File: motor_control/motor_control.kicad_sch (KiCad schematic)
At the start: 20 parts, among them J1 GPIO, J2 Conn_01x06_Pin, J3 Conn_01x06_Pin, J4 Conn_01x02_Pin, SW1 PULLUP, SW2 PULLDOWN, U1 HC-SR04

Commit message: finish up schematic
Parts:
- removed A1: RaspberryPi_Pico, Module:RaspberryPi_Pico_Common_Unspecified, symbol MCU_Module:RaspberryPi_Pico
- added A3: RaspberryPi_Pico, Module:RaspberryPi_Pico_Common_Unspecified, symbol RaspberryPi_Pico:RaspberryPi_Pico
- added J5: Conn_UART, symbol Connector:Conn_01x02_Pin
- added J6: Conn_SPI, symbol Connector:Conn_01x04_Pin
- added J7: Conn_I2C, symbol Connector:Conn_01x02_Pin
- SW1: value PULLUP -> PU
- SW2: value PULLDOWN -> PD
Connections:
- net +3V3: now also SW2.1, A3.36 (3V3(OUT)); no longer SW2.2
- net +5V: no longer U1.1 (VCC)
- net AIN1: now also A3.20 (GP15)
- net AIN2: now also A3.19 (GP14)
- net BIN1: now also A3.21 (GP16)
- net BIN2: now also A3.22 (GP17)
- net BLUE: now also A3.31 (GP26_ADC0)
- net C1A: now also A3.15 (GP11)
- net C1B: now also A3.25 (GP19)
- net C2A: now also A3.14 (GP10)
- net C2B: now also A3.26 (GP20)
- net ECHO: now also A3.12 (GP9)
- net GND: now also C1.1, A3.13 (GND), A3.18 (GND), A3.23 (GND), A3.28 (GND), A3.3 (GND), A3.33 (AGND), A3.38 (GND), A3.8 (GND); no longer C1.2
- net GREEN: now also A3.32 (GP27_ADC1)
- net PULLDOWN: now also SW2.2, A3.29 (GP22); no longer SW2.1
- net PULLUP: now also C1.2, A3.27 (GP21); no longer C1.1
- net PWMA: now also A3.17 (GP13)
- net PWMB: now also A3.24 (GP18)
- net RED: now also A3.34 (GP28_ADC2)
- net STBY: now also A3.16 (GP12)
- net TRIG: now also A3.11 (GP8)
- net VBUS: now also U1.1 (VCC), A3.40 (VBUS)
- net VSYS: now also A3.39 (VSYS)
- net GPIO2/SDA1 renamed SDA1
- net SDA1: now also A3.9 (GP6), J7.1 (Pin_1)
- net GPIO3/SCL1 renamed SCL1
- net SCL1: now also A3.10 (GP7), J7.2 (Pin_2)
- new net ADC_VREF: A3.35 (ADC_VREF)
- new net SPI0_CSn: A3.7 (GP5), J6.4 (Pin_4)
- new net SPI0_RX: A3.6 (GP4), J6.3 (Pin_3)
- new net SPI0_SCK: A3.4 (GP2), J6.1 (Pin_1)
- new net SPI0_TX: A3.5 (GP3), J6.2 (Pin_2)
- new net UART0_RX: A3.2 (GP1), J5.2 (Pin_2)
- new net UART0_TX: A3.1 (GP0), J5.1 (Pin_1)
- no-connect marks 0 -> 2
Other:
- moved on the sheet: A2, C1, C2, D1, J2, J3, J4, R1, R2, R3, R4, R5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

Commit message: assign footprints to capacitors
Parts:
- C1, C2: footprint (none) -> Capacitor_THT:C_Disc_D4.7mm_W2.5mm_P5.00mm
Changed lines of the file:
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@@
 			)
 		)
-		(property "Footprint" ""
+		(property "Footprint" "Capacitor_THT:C_Disc_D4.7mm_W2.5mm_P5.00mm"
 			(at 164.1348 149.86 0)
 			(effects
@@
 			)
 		)
-		(property "Footprint" ""
+		(property "Footprint" "Capacitor_THT:C_Disc_D4.7mm_W2.5mm_P5.00mm"
 			(at 194.6148 139.7 0)
 			(effects

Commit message: assign footprints to resistors
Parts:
- R1, R2, R3, R4, R5, R6, R7: footprint (none) -> Resistor_THT:R_Axial_DIN0207_L6.3mm_D2.5mm_P7.62mm_Horizontal
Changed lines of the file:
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@@
 			)
 		)
-		(property "Footprint" ""
+		(property "Footprint" "Resistor_THT:R_Axial_DIN0207_L6.3mm_D2.5mm_P7.62mm_Horizontal"
 			(at 231.14 150.368 90)
 			(effects
@@
 			)
 		)
-		(property "Footprint" ""
+		(property "Footprint" "Resistor_THT:R_Axial_DIN0207_L6.3mm_D2.5mm_P7.62mm_Horizontal"
 			(at 197.358 153.67 90)
 			(effects
@@
 			)
 		)
-		(property "Footprint" ""
+		(property "Footprint" "Resistor_THT:R_Axial_DIN0207_L6.3mm_D2.5mm_P7.62mm_Horizontal"
 			(at 223.52 123.952 90)
 			(effects
@@
 			)
 		)
-		(property "Footprint" ""
+		(property "Footprint" "Resistor_THT:R_Axial_DIN0207_L6.3mm_D2.5mm_P7.62mm_Horizontal"
 			(at 231.14 160.528 90)
 			(effects
@@
 			)
 		)
-		(property "Footprint" ""
+		(property "Footprint" "Resistor_THT:R_Axial_DIN0207_L6.3mm_D2.5mm_P7.62mm_Horizontal"
 			(at 223.52 129.032 90)
 			(effects
@@
 			)
 		)
-		(property "Footprint" ""
+		(property "Footprint" "Resistor_THT:R_Axial_DIN0207_L6.3mm_D2.5mm_P7.62mm_Horizontal"
 			(at 166.878 143.51 90)
 			(effects
@@
 			)
 		)
-		(property "Footprint" ""
+		(property "Footprint" "Resistor_THT:R_Axial_DIN0207_L6.3mm_D2.5mm_P7.62mm_Horizontal"
 			(at 231.14 155.448 90)
 			(effects

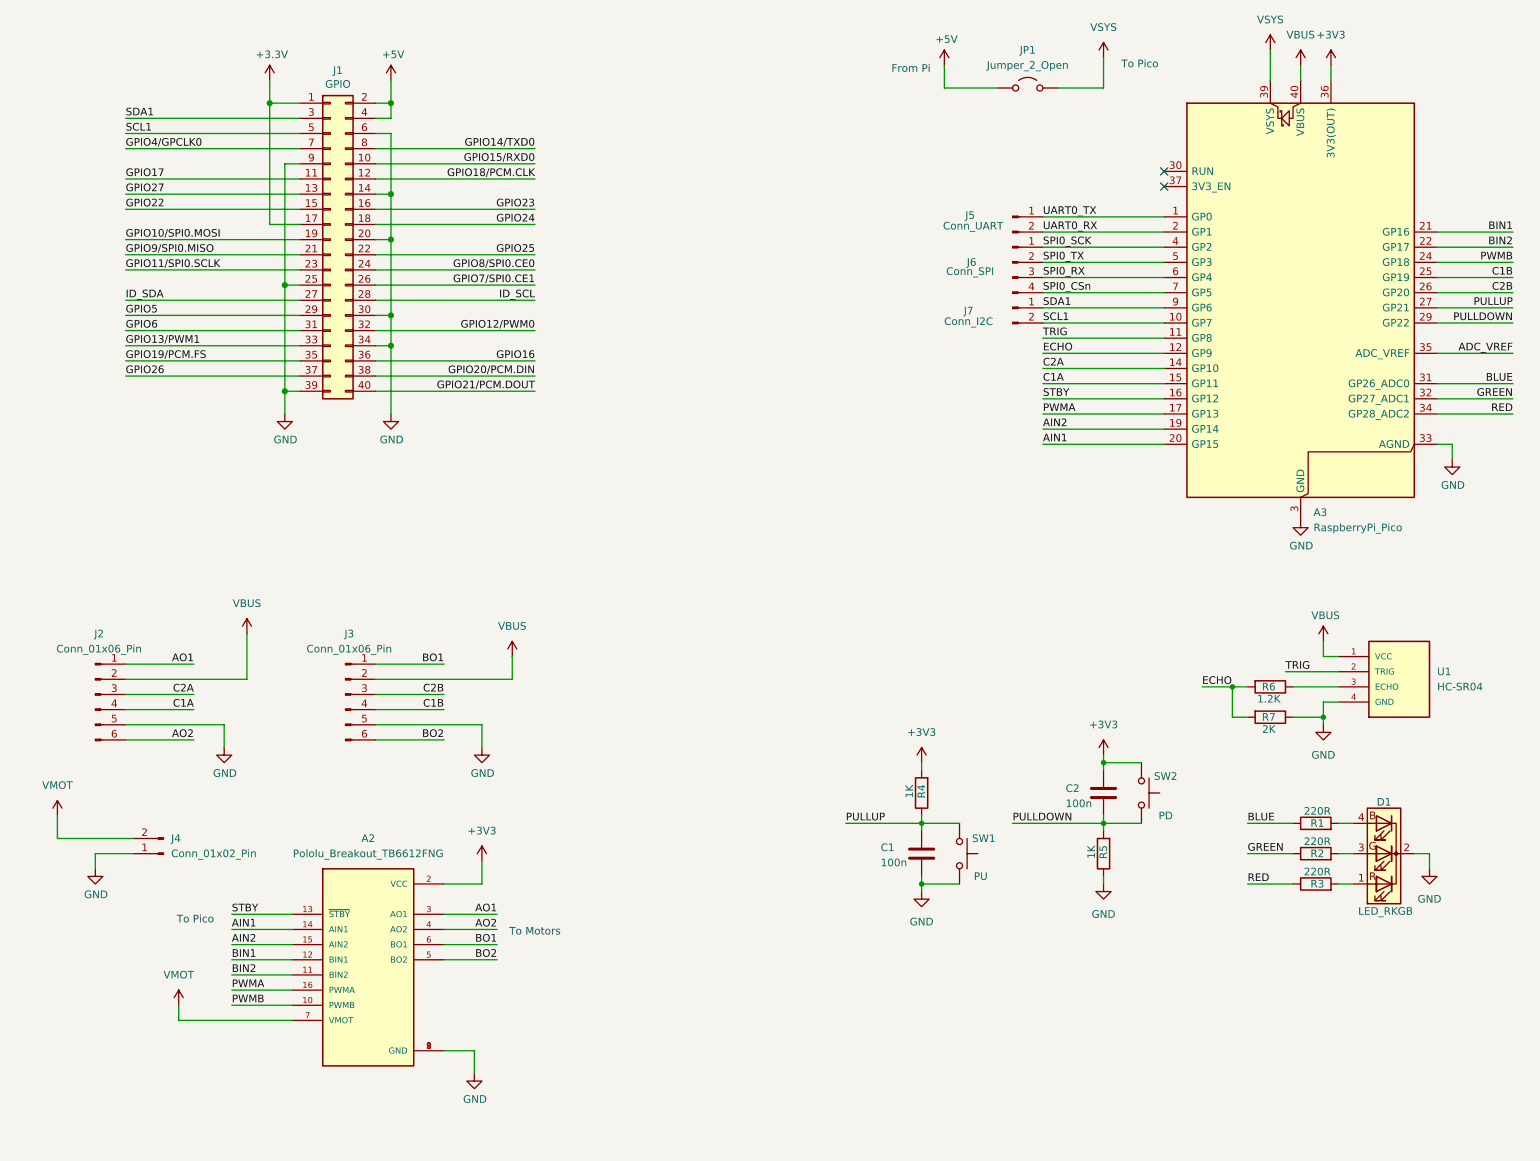
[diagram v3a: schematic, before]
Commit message: assign footprints to more parts
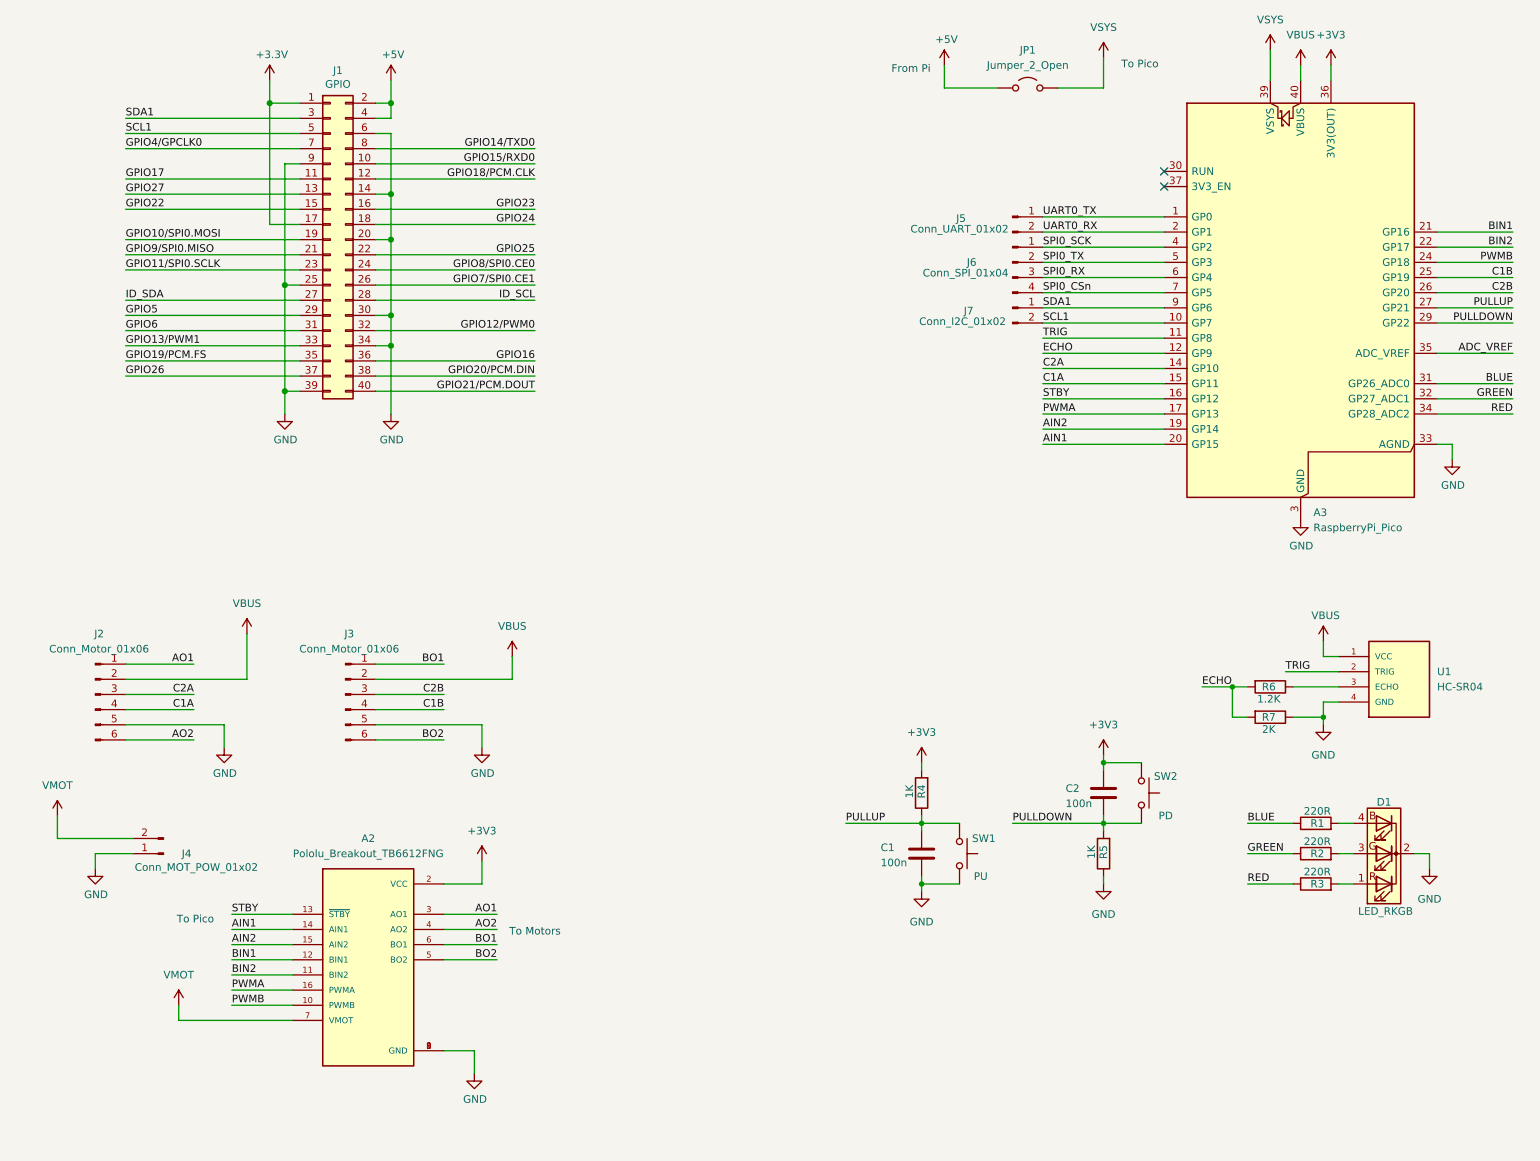
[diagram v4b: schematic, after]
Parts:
- D1: footprint (none) -> LED_THT:LED_D5.0mm-4_RGB_Wide_Pins
- J2, J3: value Conn_01x06_Pin -> Conn_Motor_01x06; footprint (none) -> Connector_PinHeader_2.54mm:PinHeader_1x06_P2.54mm_Vertical
- J4: value Conn_01x02_Pin -> Conn_MOT_POW_01x02; footprint (none) -> Connector_PinHeader_2.54mm:PinHeader_1x02_P2.54mm_Horizontal
- J5: value Conn_UART -> Conn_UART_01x02; footprint (none) -> Connector_PinHeader_2.54mm:PinHeader_1x02_P2.54mm_Vertical
- J6: value Conn_SPI -> Conn_SPI_01x04; footprint (none) -> Connector_PinHeader_2.54mm:PinHeader_1x04_P2.54mm_Vertical
- J7: value Conn_I2C -> Conn_I2C_01x02; footprint (none) -> Connector_PinHeader_2.54mm:PinHeader_1x02_P2.54mm_Vertical
- JP1: footprint (none) -> Connector_PinHeader_2.54mm:PinHeader_1x02_P2.54mm_Vertical
- SW1, SW2: footprint (none) -> Button_Switch_THT:SW_PUSH_6mm
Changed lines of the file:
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@@
 		(on_board yes)
 		(dnp no)
-		(fields_autoplaced yes)
 		(property "Reference" "J4"
-			(at 39.37 151.1299 0)
+			(at 41.148 153.67 0)
 			(effects
 				(font
@@
 			)
 		)
-		(property "Value" "Conn_01x02_Pin"
-			(at 39.37 153.6699 0)
+		(property "Value" "Conn_MOT_POW_01x02"
+			(at 33.274 155.956 0)
 			(effects
 				(font
@@
 			)
 		)
-		(property "Footprint" ""
+		(property "Footprint" "Connector_PinHeader_2.54mm:PinHeader_1x02_P2.54mm_Horizontal"
 			(at 38.1 153.67 0)
 			(effects
@@
 			)
 		)
-		(property "Footprint" ""
+		(property "Footprint" "LED_THT:LED_D5.0mm-4_RGB_Wide_Pins"
 			(at 242.57 152.4 0)
 			(effects
@@
 			)
 		)
-		(property "Value" "Conn_I2C"
-			(at 172.974 64.516 0)
-			(effects
-				(font
-					(size 1.27 1.27)
-				)
-			)
-		)
-		(property "Footprint" ""
+		(property "Value" "Conn_I2C_01x02"
+			(at 171.958 64.516 0)
+			(effects
+				(font
+					(size 1.27 1.27)
+				)
+			)
+		)
+		(property "Footprint" "Connector_PinHeader_2.54mm:PinHeader_1x02_P2.54mm_Vertical"
 			(at 180.34 62.23 0)
 			(effects
@@
 			)
 		)
-		(property "Footprint" ""
+		(property "Footprint" "Button_Switch_THT:SW_PUSH_6mm"
 			(at 207.01 143.51 0)
 			(effects
@@
 			)
 		)
-		(property "Value" "Conn_01x06_Pin"
+		(property "Value" "Conn_Motor_01x06"
 			(at 27.305 119.38 0)
 			(effects
@@
 			)
 		)
-		(property "Footprint" ""
+		(property "Footprint" "Connector_PinHeader_2.54mm:PinHeader_1x06_P2.54mm_Vertical"
 			(at 26.67 127 0)
 			(effects
@@
 		(dnp no)
 		(property "Reference" "J5"
-			(at 173.228 46.736 0)
-			(effects
-				(font
-					(size 1.27 1.27)
-				)
-			)
-		)
-		(property "Value" "Conn_UART"
-			(at 173.736 48.514 0)
-			(effects
-				(font
-					(size 1.27 1.27)
-				)
-			)
-		)
-		(property "Footprint" ""
+			(at 171.704 47.244 0)
+			(effects
+				(font
+					(size 1.27 1.27)
+				)
+			)
+		)
+		(property "Value" "Conn_UART_01x02"
+			(at 171.45 49.022 0)
+			(effects
+				(font
+					(size 1.27 1.27)
+				)
+			)
+		)
+		(property "Footprint" "Connector_PinHeader_2.54mm:PinHeader_1x02_P2.54mm_Vertical"
 			(at 180.34 46.99 0)
 			(effects
@@
 			)
 		)
-		(property "Footprint" ""
+		(property "Footprint" "Button_Switch_THT:SW_PUSH_6mm"
 			(at 176.53 153.67 0)
 			(effects
@@
 			)
 		)
-		(property "Value" "Conn_01x06_Pin"
+		(property "Value" "Conn_Motor_01x06"
 			(at 69.215 119.38 0)
 			(effects
@@
 			)
 		)
-		(property "Footprint" ""
+		(property "Footprint" "Connector_PinHeader_2.54mm:PinHeader_1x06_P2.54mm_Vertical"
 			(at 68.58 127 0)
 			(effects
@@
 			)
 		)
-		(property "Footprint" ""
+		(property "Footprint" "Connector_PinHeader_2.54mm:PinHeader_1x02_P2.54mm_Vertical"
 			(at 182.88 25.4 0)
 			(effects
@@
 			)
 		)
-		(property "Value" "Conn_SPI"
-			(at 173.228 56.134 0)
-			(effects
-				(font
-					(size 1.27 1.27)
-				)
-			)
-		)
-		(property "Footprint" ""
+		(property "Value" "Conn_SPI_01x04"
+			(at 172.466 56.388 0)
+			(effects
+				(font
+					(size 1.27 1.27)
+				)
+			)
+		)
+		(property "Footprint" "Connector_PinHeader_2.54mm:PinHeader_1x04_P2.54mm_Vertical"
 			(at 180.34 54.61 0)
 			(effects

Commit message: assign all footprints
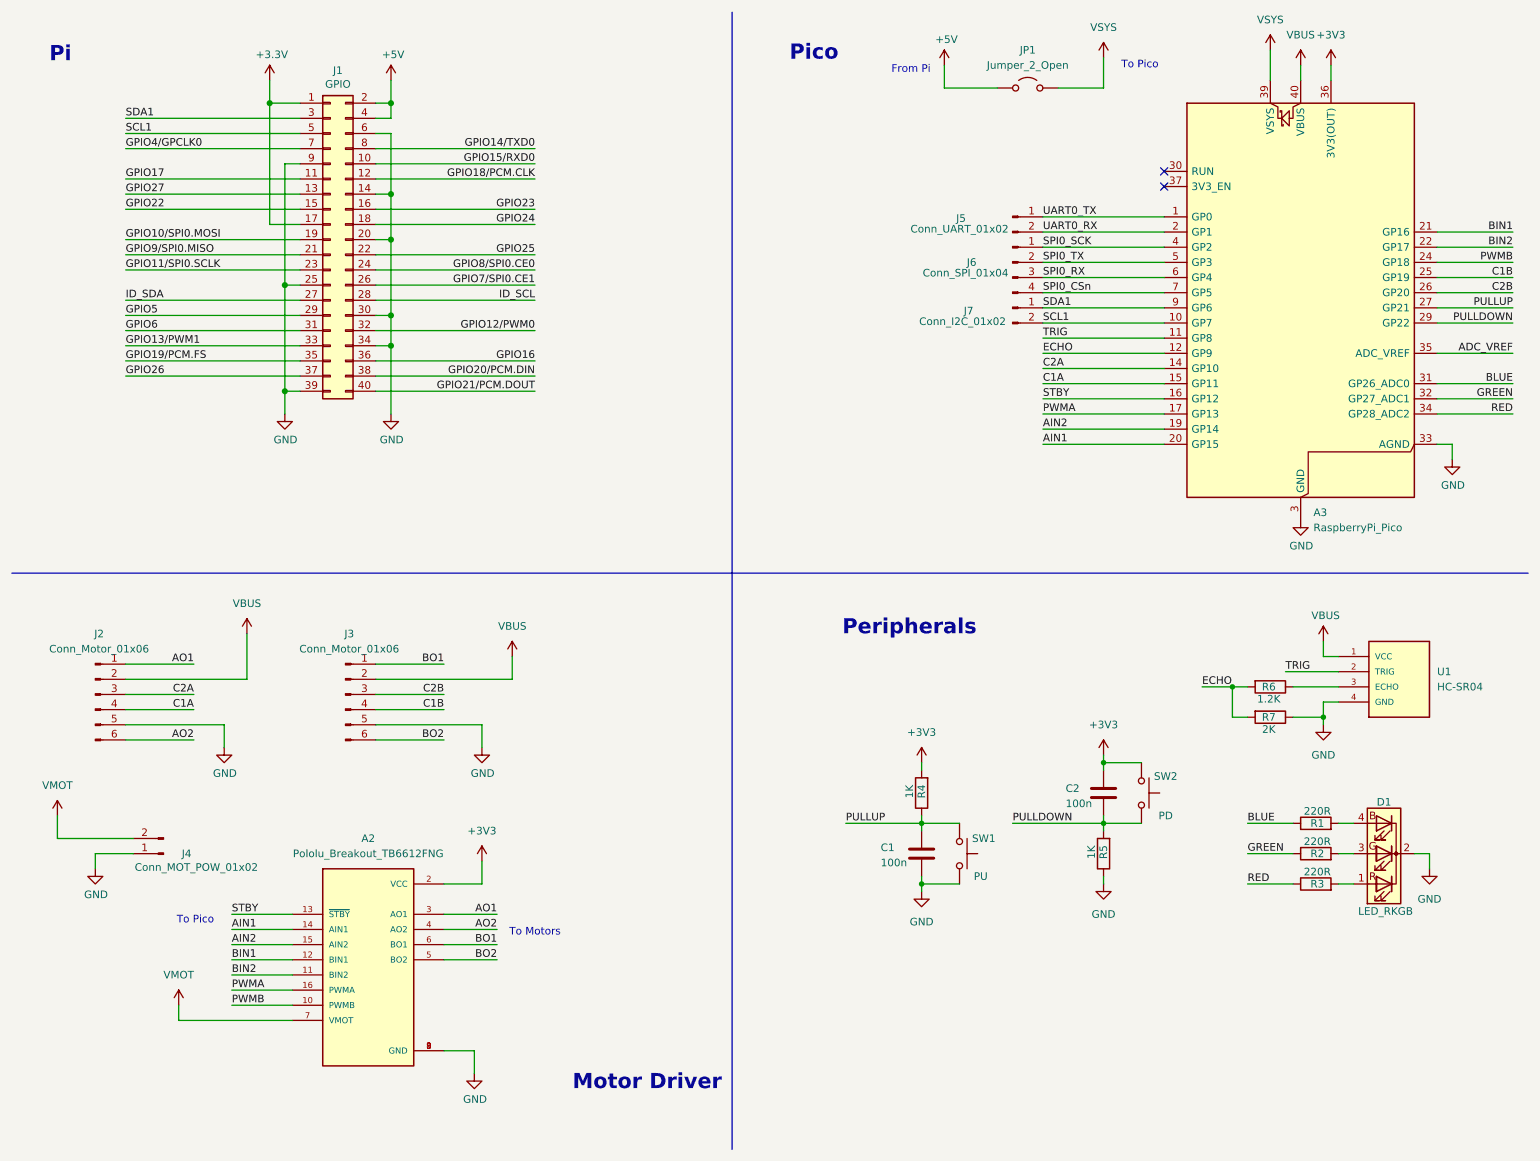
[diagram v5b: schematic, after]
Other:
- note added: "Motor Driver"
- note added: "Peripherals"
- note added: "Pi"
- note added: "Pico"
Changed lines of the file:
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@@
 		(company "UCA")
+	)
+	(text "Pico"
+		(exclude_from_sim no)
+		(at 147.066 19.558 0)
+		(effects
+			(font
+				(size 2.54 2.54)
+				(thickness 0.508)
+				(bold yes)
+				(color 144 32 255 1)
+			)
+		)
 	)
 	(text "From Pi"
@@
 		)
 	)
+	(text "Peripherals"
+		(exclude_from_sim no)
+		(at 163.068 115.824 0)
+		(effects
+			(font
+				(size 2.54 2.54)
+				(thickness 0.508)
+				(bold yes)
+				(color 144 32 255 1)
+			)
+		)
+	)
 	(text "To Pico"
 		(exclude_from_sim no)
@@
 		)
 	)
+	(text "Motor Driver"
+		(exclude_from_sim no)
+		(at 119.126 192.024 0)
+		(effects
+			(font
+				(size 2.54 2.54)
+				(thickness 0.508)
+				(bold yes)
+				(color 144 32 255 1)
+			)
+		)
+	)
 	(text "To Pico"
 		(exclude_from_sim no)
@@
 		)
 	)
+	(text "Pi"
+		(exclude_from_sim no)
+		(at 20.828 19.812 0)
+		(effects
+			(font
+				(size 2.54 2.54)
+				(thickness 0.508)
+				(bold yes)
+				(color 144 32 255 1)
+			)
+		)
+	)
 	(junction
 		(at 195.58 138.43)
@@
 		)
 	)
+	(polyline
+		(pts
+			(xy 12.7 106.68) (xy 266.7 106.68)
+		)
+		(stroke
+			(width 0)
+			(type default)
+		)
+	)
 	(wire
 		(pts
@@
 		)
 		(stroke
+			(width 0)
+			(type default)
+		)
+	)
+	(polyline
+		(pts
+			(xy 133.35 12.7) (xy 133.35 203.2)
+		)
+		(stroke

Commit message: layout v1
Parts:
- added J8: VBUS_OUT, Connector_PinHeader_2.54mm:PinHeader_1x02_P2.54mm_Vertical, symbol Connector:Conn_01x02_Pin
- J2: value Conn_Motor_01x06 -> MotA
- J3: value Conn_Motor_01x06 -> MotB
- J4: value Conn_MOT_POW_01x02 -> MOT_POW
- J5: value Conn_UART_01x02 -> UART
- J6: value Conn_SPI_01x04 -> SPI
- J7: value Conn_I2C_01x02 -> I2C
- JP1: value Jumper_2_Open -> 5V_VBUS
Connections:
- net GND: now also J8.2 (Pin_2)
- net VBUS: now also J8.1 (Pin_1)
